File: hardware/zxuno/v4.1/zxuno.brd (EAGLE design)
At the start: 86 x 56 mm, 103 parts, among them T1 BC846, U1 6SLX9TQG144, U2 FLASH-SPI-25XXSMD1, U4 AD724, U5 50MHz, U6 3.3V, U7 1.2V, Y1 3.58M, Y2 4.43M

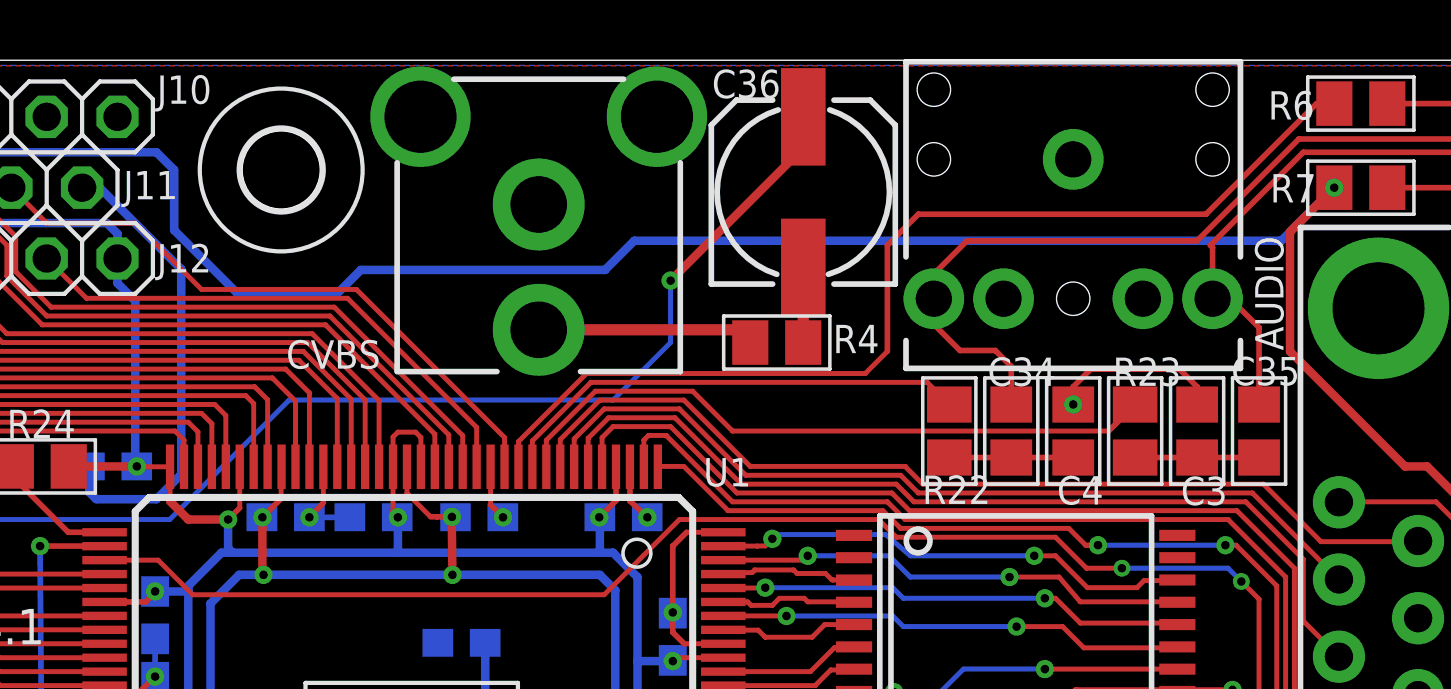
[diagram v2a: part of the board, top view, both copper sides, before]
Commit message: 6- RCA video compuesto: El agujero de la pata trasera es del mismo tamaño que la pata. No entra y hay que limar 0.5mm para que entre
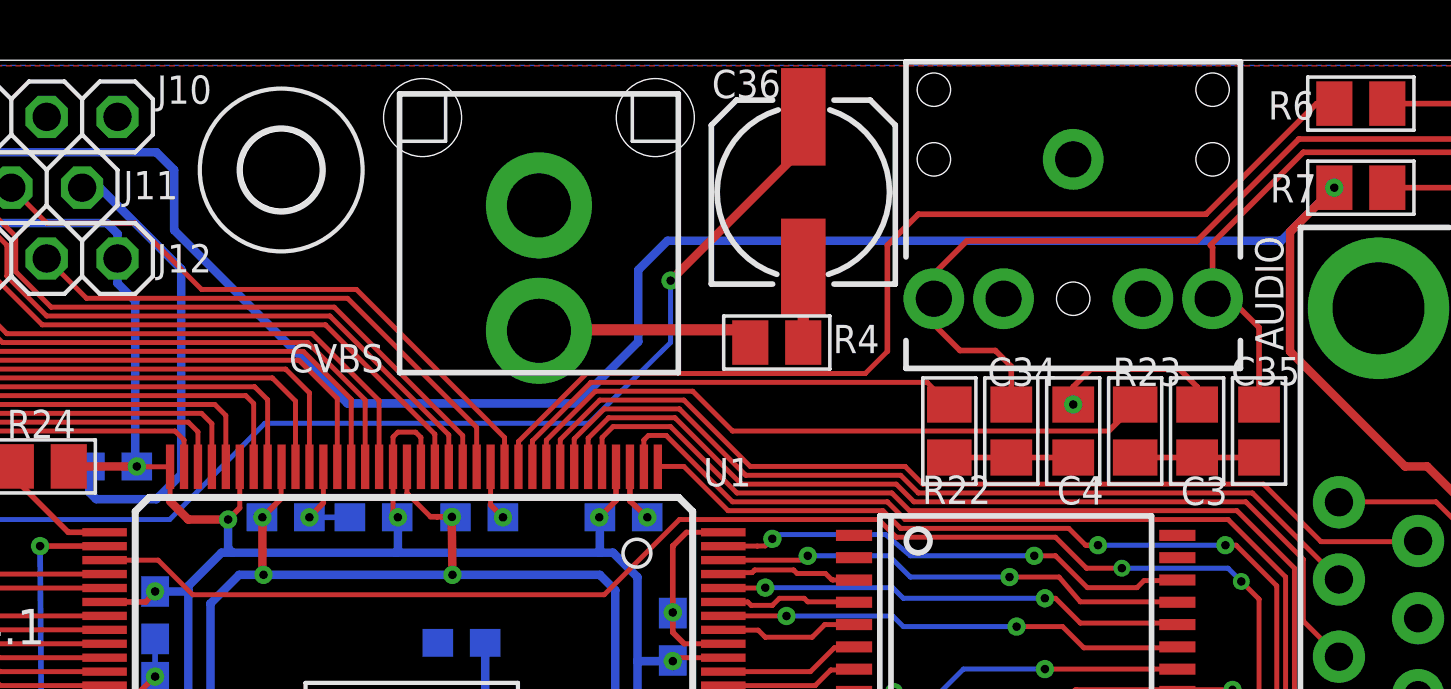
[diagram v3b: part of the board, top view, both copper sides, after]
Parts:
- CVBS: device ZX_UNO_0_15:RCA_JACK_RCJ-04X_-_DUPLICATE_1PRIMARY -> uzebox:RCA
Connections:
- net GND: now also CVBS.GND; no longer CVBS.4
- net N$28: now also CVBS.SIG; no longer CVBS.3
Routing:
- net 5V: track 228.6 -> 233.3 mm
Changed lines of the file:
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@@
 <attribute name="VALUE" x="85.66785" y="18.3388" size="2.032" layer="27" font="vector" ratio="13" rot="SR270"/>
-</element>
-<element name="CVBS" library="ZX_UNO_0_15" package="RCA_JACK_RCJ-04X_-_DUPLICATE_1PRIMARY" value="RCA" x="46.228" y="50.83175" smashed="yes">
-<attribute name="NAME" x="37.164875" y="44.943575" size="1.016" layer="25" font="vector" ratio="15" rot="SR0"/>
-<attribute name="VALUE" x="40.677996875" y="55.42115" size="2.032" layer="27" font="vector" ratio="13" rot="SR0"/>
 </element>
 <element name="U5" library="ZX_UNO_0_15" package="SM/OSC_1PRIMARY" value="50MHz" x="44.211875" y="28.2575" smashed="yes" rot="MR180">
@@
 </element>
 <element name="J16" library="pinhead" package="2X02" value="" x="69.69125" y="17.30375" rot="R180"/>
+<element name="CVBS" library="uzebox" package="RCA" value="RCA" x="46.2359375" y="50.8" smashed="yes">
+<attribute name="NAME" x="37.2665625" y="44.8071875" size="1.016" layer="25" font="vector" ratio="15"/>
+</element>
 </elements>
 <signals>
@@
 <wire x1="69.215" y1="44.92625" x2="69.85" y2="44.29125" width="0.2032" layer="1"/>
 <wire x1="69.85" y1="44.29125" x2="69.85" y2="43.65375" width="0.2032" layer="1"/>
-<contactref element="CVBS" pad="4"/>
 <wire x1="13.6525" y1="31.115" x2="14.44375" y2="31.115" width="0.1778" layer="1"/>
 <wire x1="71.060625" y1="30.959375" x2="71.12" y2="30.933125" width="0.2032" layer="1"/>
@@
 <wire x1="3.4053125" y1="2.81" x2="5.000625" y2="4.4053125" width="0.2032" layer="1"/>
 <wire x1="5.000625" y1="4.4053125" x2="5.000625" y2="5.9436" width="0.2032" layer="1"/>
+<contactref element="CVBS" pad="GND"/>
 </signal>
 <signal name="XD0">
@@
 <wire x1="77.62875" y1="18.0975" x2="77.62875" y2="15.39875" width="0.3048" layer="1"/>
 <wire x1="77.62875" y1="15.39875" x2="77.62875" y2="15.24" width="0.3048" layer="1"/>
-<wire x1="49.657" y1="49.53" x2="48.60925" y2="48.48225" width="0.3048" layer="16"/>
-<wire x1="48.60925" y1="48.48225" x2="39.84625" y2="48.48225" width="0.3048" layer="16"/>
-<wire x1="39.84625" y1="48.48225" x2="38.989" y2="47.625" width="0.3048" layer="16"/>
-<wire x1="38.989" y1="47.625" x2="35.433" y2="47.625" width="0.3048" layer="16"/>
-<wire x1="35.433" y1="47.625" x2="33.147" y2="49.911" width="0.3048" layer="16"/>
+<wire x1="50.847625" y1="49.53" x2="49.799875" y2="48.48225" width="0.3048" layer="16"/>
 <wire x1="33.147" y1="49.911" x2="33.147" y2="52.07" width="0.3048" layer="16"/>
 <wire x1="33.147" y1="52.07" x2="32.512" y2="52.705" width="0.3048" layer="16"/>
@@
 <wire x1="3.81" y1="52.705" x2="3.175" y2="52.07" width="0.3048" layer="16"/>
 <wire x1="3.175" y1="52.07" x2="3.175" y2="48.895" width="0.3048" layer="16"/>
-<wire x1="49.657" y1="49.53" x2="72.80275" y2="49.53" width="0.3048" layer="16"/>
+<wire x1="50.847625" y1="49.53" x2="72.80275" y2="49.53" width="0.3048" layer="16"/>
 <wire x1="72.80275" y1="49.53" x2="72.8345" y2="49.49825" width="0.3048" layer="16"/>
 <wire x1="16.88465" y1="27.17165" x2="16.88465" y2="23.7846" width="0.4064" layer="1"/>
@@
 <wire x1="78.105" y1="41.43375" x2="77.31125" y2="41.43375" width="0.3048" layer="1"/>
 <wire x1="77.31125" y1="41.43375" x2="73.18375" y2="45.56125" width="0.3048" layer="1"/>
+<wire x1="49.799875" y1="48.48225" x2="49.799875" y2="45.9105" width="0.3048" layer="16"/>
+<wire x1="49.799875" y1="45.9105" x2="47.5853125" y2="43.6959375" width="0.3048" layer="16"/>
+<wire x1="47.5853125" y1="43.6959375" x2="39.3620625" y2="43.6959375" width="0.3048" layer="16"/>
+<wire x1="39.3620625" y1="43.6959375" x2="33.147" y2="49.911" width="0.3048" layer="16"/>
 </signal>
 <signal name="N$14">
@@
 <wire x1="55.72125" y1="53.97625" x2="55.405" y2="53.97625" width="0.3048" layer="1"/>
 <via x="50.95875" y="48.10125" extent="1-16" drill="0.3048" diameter="0.6604"/>
-<wire x1="37.2745" y1="43.815" x2="32.98825" y2="39.52875" width="0.1778" layer="16"/>
+<wire x1="36.401375" y1="42.9815625" x2="32.98825" y2="39.52875" width="0.1778" layer="16"/>
 <wire x1="32.98825" y1="39.52875" x2="16.51" y2="39.52875" width="0.1778" layer="16"/>
 <wire x1="16.51" y1="39.52875" x2="7.064375" y2="30.083125" width="0.1778" layer="16"/>
@@
 <via x="14.12875" y="15.24" extent="1-16" drill="0.3048" diameter="0.6604"/>
 <wire x1="14.12875" y1="15.24" x2="16.19625" y2="15.24" width="0.3048" layer="1"/>
-<wire x1="37.2745" y1="43.815" x2="48.895" y2="43.815" width="0.1778" layer="16"/>
-<wire x1="48.895" y1="43.815" x2="50.95875" y2="45.87875" width="0.1778" layer="16"/>
+<wire x1="36.401375" y1="42.9815625" x2="48.021875" y2="42.9815625" width="0.1778" layer="16"/>
+<wire x1="48.021875" y1="42.9815625" x2="50.95875" y2="45.87875" width="0.1778" layer="16"/>
 <wire x1="50.95875" y1="48.10125" x2="50.95875" y2="45.87875" width="0.1778" layer="16"/>
 <wire x1="50.95875" y1="48.10125" x2="55.72125" y2="52.86375" width="0.3048" layer="1"/>
@@
 <signal name="N$28">
 <contactref element="R4" pad="2"/>
-<contactref element="CVBS" pad="3"/>
-<wire x1="46.228" y1="46.33595" x2="53.36155" y2="46.33595" width="0.4064" layer="1"/>
 <wire x1="53.36155" y1="46.33595" x2="53.81875" y2="45.87875" width="0.4064" layer="1"/>
+<contactref element="CVBS" pad="SIG"/>
+<wire x1="53.36155" y1="46.33595" x2="46.2718875" y2="46.33595" width="0.4064" layer="1"/>
+<wire x1="46.2718875" y1="46.33595" x2="46.2359375" y2="46.3" width="0.4064" layer="1"/>
 </signal>
 <signal name="N$31">

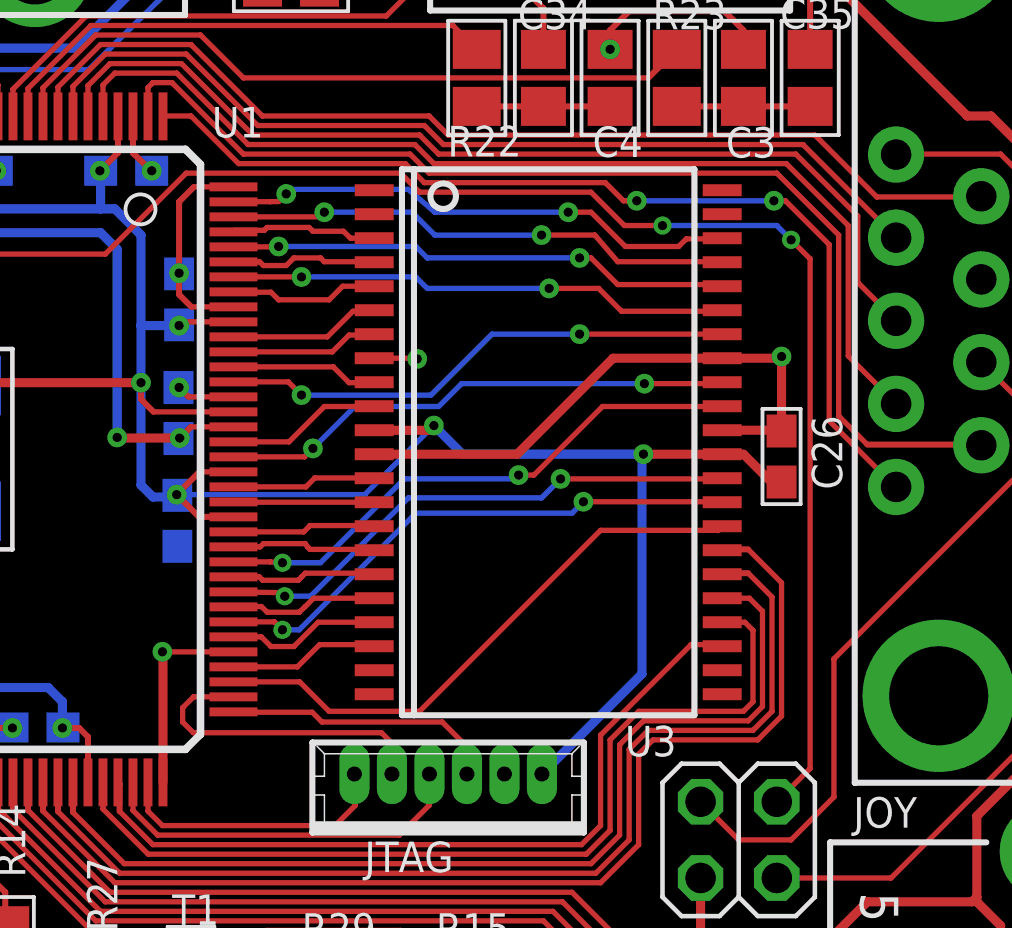
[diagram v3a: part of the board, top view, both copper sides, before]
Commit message: Quito vías por la zona de SRAM
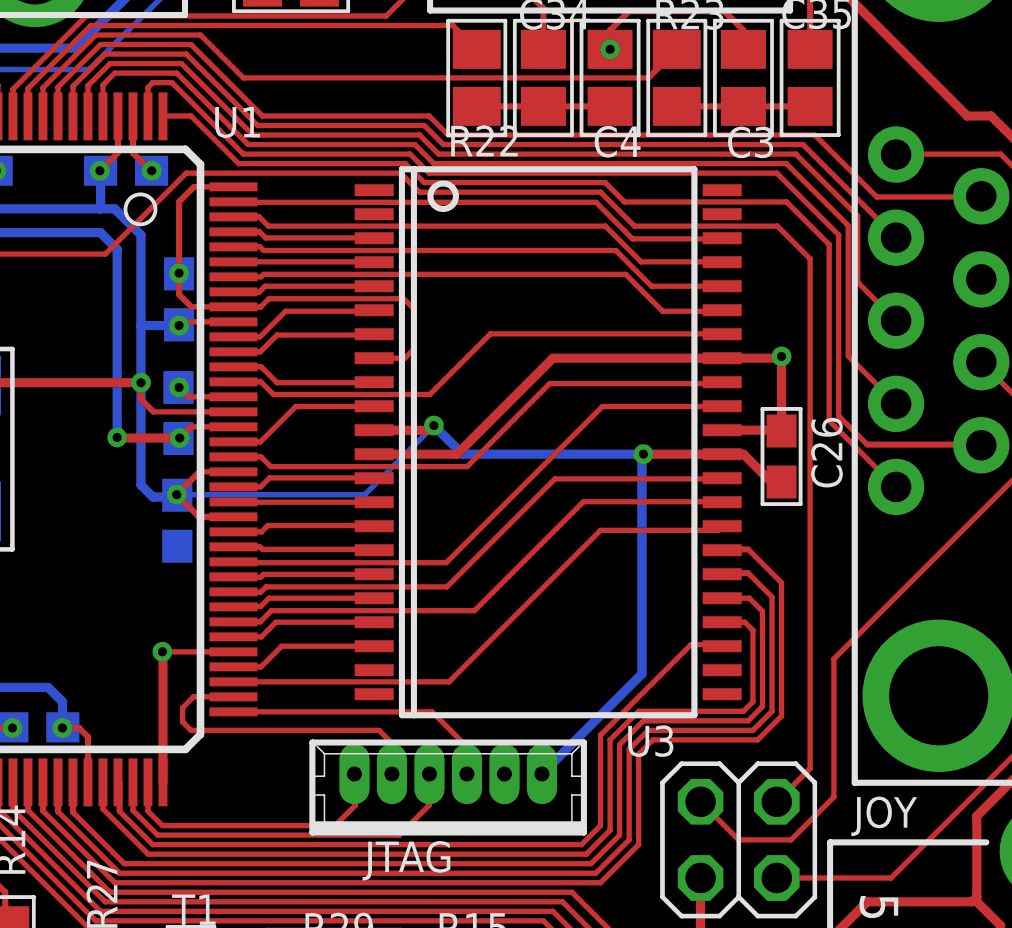
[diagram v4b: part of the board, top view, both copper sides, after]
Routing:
- net GND: track 141.4 -> 149.1 mm, vias 26 -> 25
- net XA14: track 19.3 -> 18.4 mm
- net XA20: track 17.3 -> 16.8 mm, vias 2 -> 0
- net XD7: track 17.3 -> 17.6 mm, vias 2 -> 0
- net XD4: track 18.2 -> 18.0 mm, vias 2 -> 0
- net XA18: track 17.1 -> 16.9 mm, vias 2 -> 0
- net XD5: track 18.0 -> 17.9 mm, vias 2 -> 0
- net XA16: vias 2 -> 0
- net XD6: vias 2 -> 0
- net XA15: vias 2 -> 0
- net JOY_UP: vias 2 -> 0
- net JOY_FIRE3: vias 2 -> 0
- net XA17: vias 2 -> 0
